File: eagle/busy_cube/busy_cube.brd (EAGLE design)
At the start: 108 x 41.9 mm, 14 parts

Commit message: Code used in first version of the box
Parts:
- R1: value 500 -> 470
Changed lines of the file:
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@@
 </element>
 <element name="NEO_PIXELS" library="busy_cube_lib" package="1X03_LONGPADS" value="" x="3.81" y="26.67" rot="R270"/>
-<element name="R1" library="busy_cube_lib" package="AXIAL-0.3" value=" 500" x="25.4" y="25.4" rot="R90">
+<element name="R1" library="busy_cube_lib" package="AXIAL-0.3" value="470" x="25.4" y="25.4" rot="R90">
 <attribute name="PROD_ID" value=" " x="25.4" y="25.4" size="1.778" layer="27" rot="R90" display="off"/>
 </element>

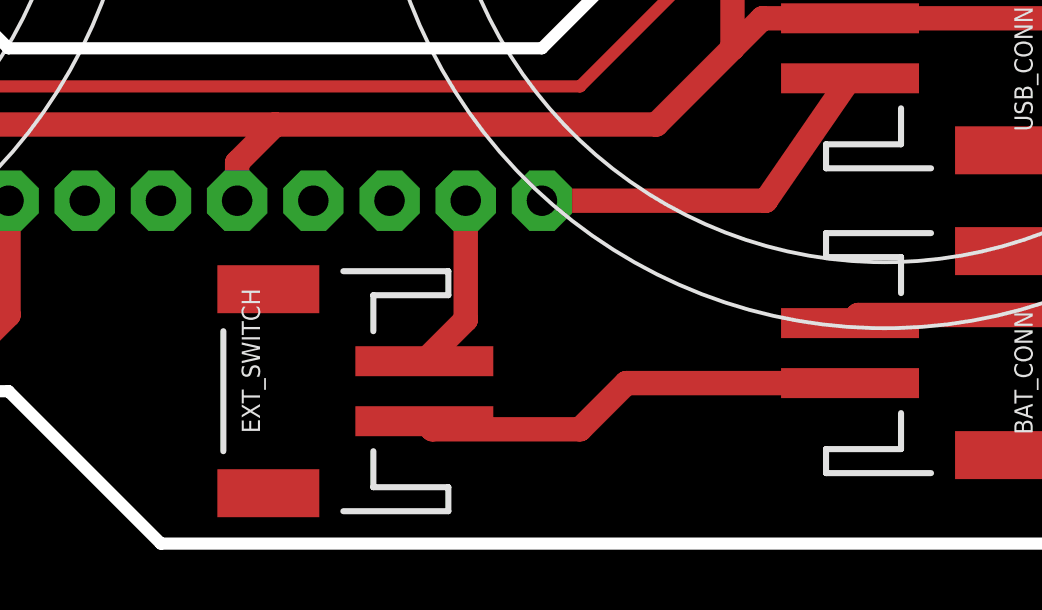
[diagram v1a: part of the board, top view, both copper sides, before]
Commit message: Switch is now connected to the EN pin
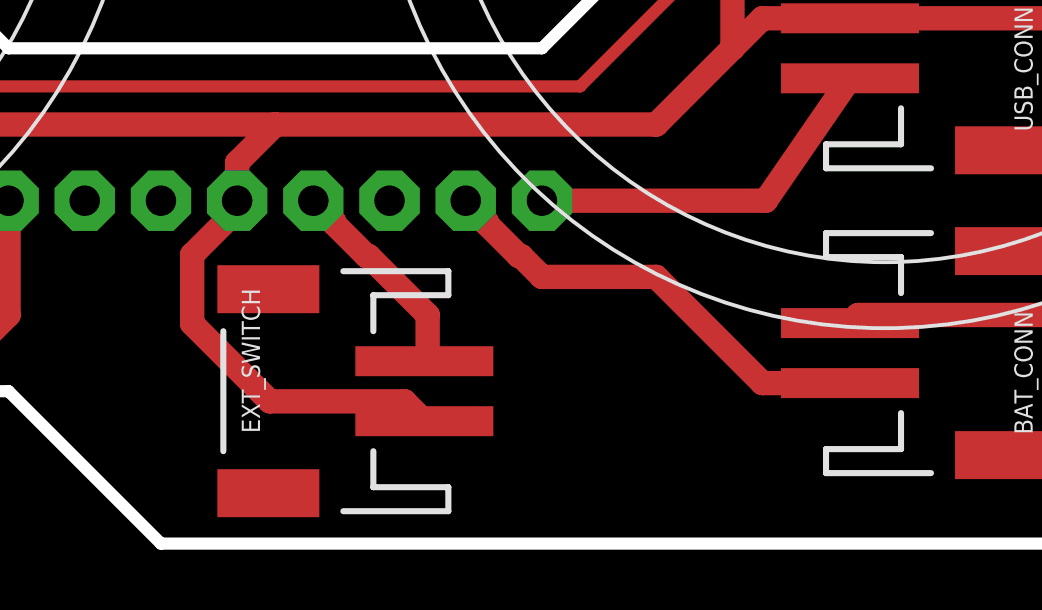
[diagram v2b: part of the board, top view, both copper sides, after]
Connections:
- net BAT_IN_VCC: now also BAT_CONN.2; no longer EXT_SWITCH.2
- net GND: now also EXT_SWITCH.1
- net N$10: now also EXT_SWITCH.2, POWERBOOST.EN; no longer BAT_CONN.2, EXT_SWITCH.1
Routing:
- net GND: track 178.4 -> 192.2 mm
- net BAT_IN_VCC: track 5.92 -> 15.4 mm
- net N$10: track 14.9 -> 7.02 mm
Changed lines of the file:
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@@
 <?xml version="1.0" encoding="utf-8"?>
 <!DOCTYPE eagle SYSTEM "eagle.dtd">
-<eagle version="8.3.2">
+<eagle version="8.5.2">
 <drawing>
 <settings>
@@
 <param name="dpMaxLengthDifference" value="10mm"/>
 <param name="dpGapFactor" value="2.5"/>
-<param name="checkGrid" value="0"/>
 <param name="checkAngle" value="0"/>
 <param name="checkFont" value="1"/>
 <param name="checkRestrict" value="1"/>
+<param name="checkStop" value="0"/>
+<param name="checkValues" value="0"/>
 <param name="useDiameter" value="13"/>
 <param name="maxErrors" value="50"/>
@@
 <wire x1="28.5162" y1="19.7438" x2="28.445275" y2="19.7438" width="0.8128" layer="1"/>
 <wire x1="27.3638" y1="20.825275" x2="27.3638" y2="23.4362" width="0.8128" layer="1"/>
+<contactref element="EXT_SWITCH" pad="1"/>
+<wire x1="82.44" y1="4.08" x2="81.7782" y2="4.7418" width="0.8128" layer="1"/>
+<wire x1="74.7018" y1="7.33280625" x2="74.7018" y2="9.62719375" width="0.8128" layer="1"/>
+<wire x1="76.2" y1="11.12539375" x2="76.2" y2="11.43" width="0.8128" layer="1"/>
+<wire x1="74.7018" y1="9.62719375" x2="76.2" y2="11.12539375" width="0.8128" layer="1"/>
+<wire x1="81.7782" y1="4.7418" x2="77.29280625" y2="4.7418" width="0.8128" layer="1"/>
+<wire x1="77.29280625" y1="4.7418" x2="74.7018" y2="7.33280625" width="0.8128" layer="1"/>
 </signal>
 <signal name="VCC">
@@
 <signal name="BAT_IN_VCC">
 <contactref element="POWERBOOST" pad="BAT"/>
-<contactref element="EXT_SWITCH" pad="2"/>
-<wire x1="82.44" y1="6.08" x2="83.82" y2="7.46" width="0.8128" layer="1"/>
-<wire x1="83.82" y1="7.46" x2="83.82" y2="11.43" width="0.8128" layer="1"/>
+<contactref element="BAT_CONN" pad="2"/>
+<wire x1="83.82" y1="11.43" x2="84.5138" y2="10.7362" width="0.8128" layer="1"/>
+<wire x1="84.5138" y1="10.7362" x2="84.5138" y2="10.665275" width="0.8128" layer="1"/>
+<wire x1="84.5138" y1="10.665275" x2="85.595275" y2="9.5838" width="0.8128" layer="1"/>
+<wire x1="85.595275" y1="9.5838" x2="85.6662" y2="9.5838" width="0.8128" layer="1"/>
+<wire x1="85.6662" y1="9.5838" x2="86.36" y2="8.89" width="0.8128" layer="1"/>
+<wire x1="86.36" y1="8.89" x2="90.17" y2="8.89" width="0.8128" layer="1"/>
+<wire x1="90.17" y1="8.89" x2="93.71" y2="5.35" width="0.8128" layer="1"/>
+<wire x1="93.71" y1="5.35" x2="96.63" y2="5.35" width="0.8128" layer="1"/>
 </signal>
 <signal name="NEO_RES">
@@
 <wire x1="45.72" y1="12.7" x2="46.99" y2="11.43" width="0.4064" layer="1"/>
 <wire x1="46.99" y1="11.43" x2="50.84" y2="11.43" width="0.4064" layer="1"/>
-</signal>
-<signal name="N$10">
-<contactref element="BAT_CONN" pad="2"/>
-<contactref element="EXT_SWITCH" pad="1"/>
-<wire x1="96.63" y1="5.35" x2="89.17" y2="5.35" width="0.8128" layer="1"/>
-<wire x1="89.17" y1="5.35" x2="87.63" y2="3.81" width="0.8128" layer="1"/>
-<wire x1="87.63" y1="3.81" x2="82.71" y2="3.81" width="0.8128" layer="1"/>
-<wire x1="82.71" y1="3.81" x2="82.44" y2="4.08" width="0.8128" layer="1"/>
 </signal>
 <signal name="N$11">
@@
 <wire x1="30.26355625" y1="40.64" x2="38.1" y2="40.64" width="0.4064" layer="1"/>
 </signal>
+<signal name="N$10">
+<contactref element="POWERBOOST" pad="EN"/>
+<contactref element="EXT_SWITCH" pad="2"/>
+<wire x1="78.74" y1="11.43" x2="79.4338" y2="10.7362" width="0.8128" layer="1"/>
+<wire x1="79.4338" y1="10.7362" x2="79.4338" y2="10.665275" width="0.8128" layer="1"/>
+<wire x1="79.4338" y1="10.665275" x2="80.515275" y2="9.5838" width="0.8128" layer="1"/>
+<wire x1="80.515275" y1="9.5838" x2="80.5862" y2="9.5838" width="0.8128" layer="1"/>
+<wire x1="80.5862" y1="9.5838" x2="82.55" y2="7.62" width="0.8128" layer="1"/>
+<wire x1="82.55" y1="7.62" x2="82.55" y2="6.19" width="0.8128" layer="1"/>
+<wire x1="82.55" y1="6.19" x2="82.44" y2="6.08" width="0.8128" layer="1"/>
+</signal>
 </signals>
